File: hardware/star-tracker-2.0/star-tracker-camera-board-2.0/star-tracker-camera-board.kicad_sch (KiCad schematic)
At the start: 41 parts, among them J1 3-1734742-6, U1 AR0134CSSM00SPCA0, U2 TPS70618DRVR, U3 TPS71928-28DRVT, U4 TPS71928-28DRVT, X1 MC2520Z27.0000C19XSH

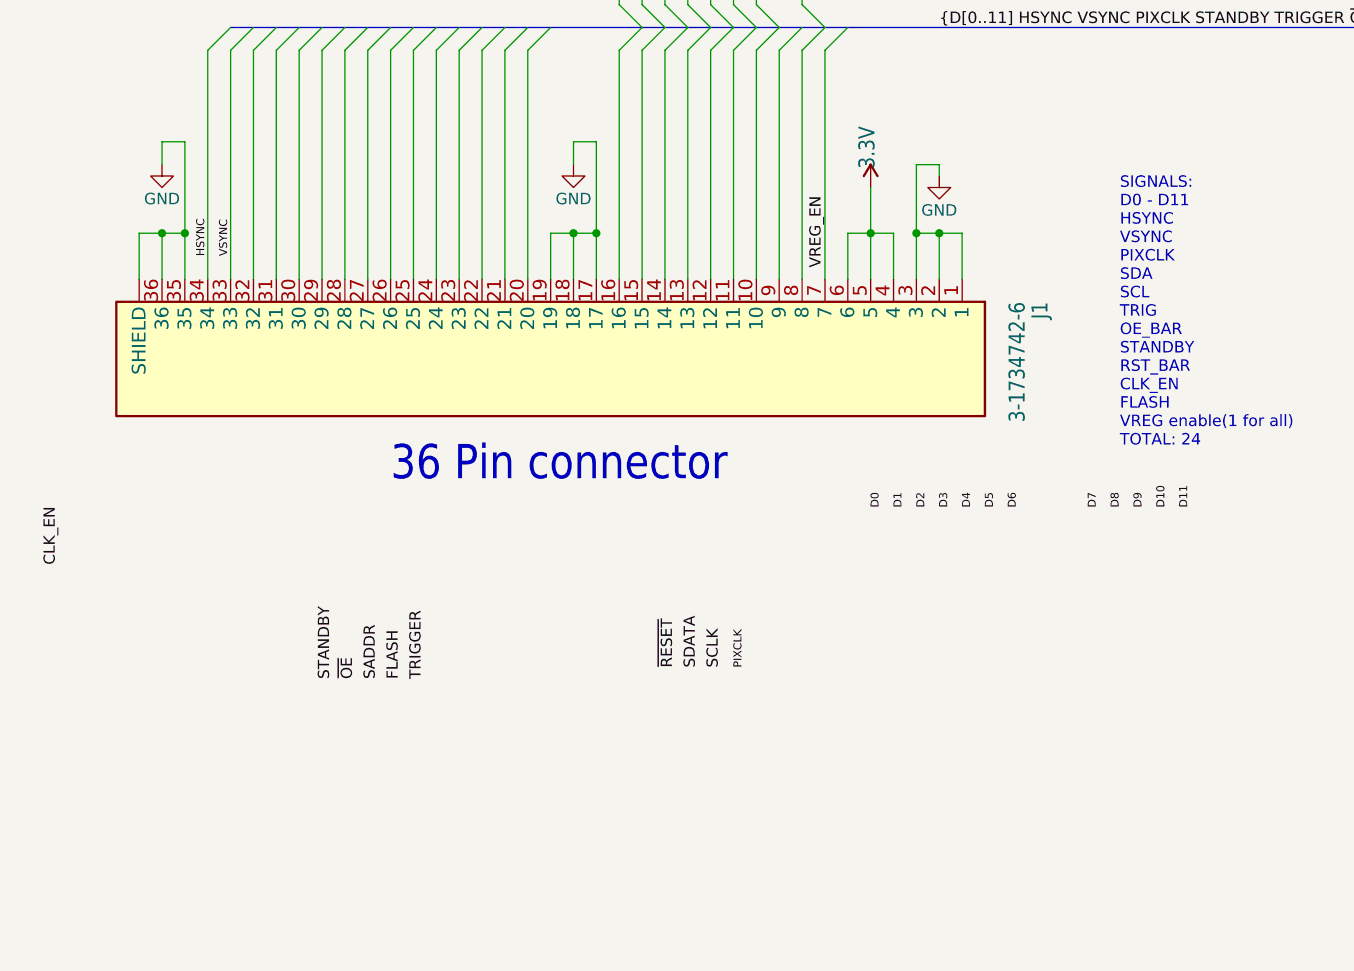
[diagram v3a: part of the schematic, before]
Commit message: Update on camera board
Finished layout and routing. Only needs DRC error fixing and silk screen placement
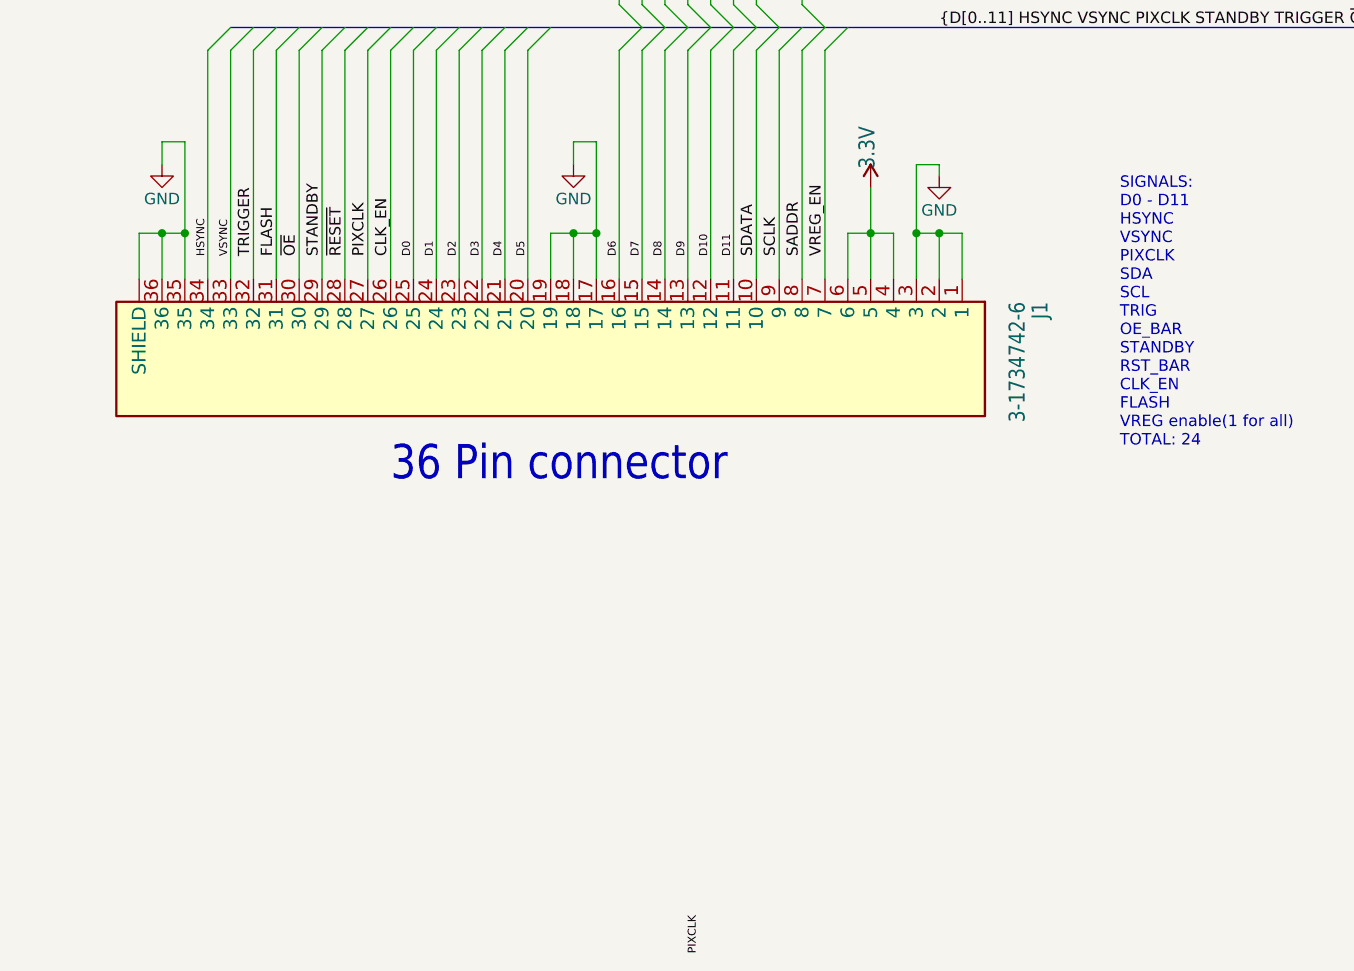
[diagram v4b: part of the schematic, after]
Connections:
- net CLK_EN: now also J1.26
- net D0: now also J1.25
- net D1: now also J1.24
- net D10: now also J1.12
- net D11: now also J1.11
- net D2: now also J1.23
- net D3: now also J1.22
- net D4: now also J1.21
- net D5: now also J1.20
- net D6: now also J1.16
- net D7: now also J1.15
- net D8: now also J1.14
- net D9: now also J1.13
- net FLASH: now also J1.31
- net PIXCLK: now also J1.27
- net SADDR: now also J1.8
- net SCLK: now also J1.9
- net SDATA: now also J1.10
- net STANDBY: now also J1.29
- net TRIGGER: now also J1.32
- net ~{OE}: now also J1.30
- net ~{RESET}: now also J1.28
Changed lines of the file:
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@@
 	(wire
 		(pts
+			(xy 137.16 170.18) (xy 137.16 195.58)
+		)
+		(stroke
+			(width 0.1524)
+			(type solid)
+		)
+	)
+	(wire
+		(pts
 			(xy 116.84 66.04) (xy 116.84 76.2)
 		)
@@
 	(wire
 		(pts
-			(xy 134.62 170.18) (xy 134.62 195.58)
-		)
-		(stroke
-			(width 0)
-			(type default)
-		)
-	)
-	(wire
-		(pts
 			(xy 294.64 53.34) (xy 294.64 55.88)
 		)
@@
 	(wire
 		(pts
-			(xy 137.16 170.18) (xy 137.16 195.58)
-		)
-		(stroke
-			(width 0.1524)
-			(type solid)
-		)
-	)
-	(wire
-		(pts
 			(xy 368.3 134.62) (xy 368.3 132.08)
 		)
@@
 	(wire
 		(pts
+			(xy 134.62 170.18) (xy 134.62 195.58)
+		)
+		(stroke
+			(width 0)
+			(type default)
+		)
+	)
+	(wire
+		(pts
 			(xy 144.78 134.62) (xy 144.78 132.08)
 		)
@@
 		)
 	)
-	(label "D3"
-		(at 151.13 220.98 90)
-		(effects
-			(font
-				(size 0.889 0.889)
-			)
-			(justify left bottom)
-		)
-	)
-	(label "D0"
-		(at 143.51 220.98 90)
-		(effects
-			(font
-				(size 0.889 0.889)
-			)
-			(justify left bottom)
-		)
-	)
 	(label "D0"
 		(at 231.14 73.66 0)
@@
 		)
 	)
-	(label "PIXCLK"
-		(at 128.27 238.76 90)
-		(effects
-			(font
-				(size 0.889 0.889)
-			)
-			(justify left bottom)
-		)
-	)
 	(label "SCLK"
 		(at 166.37 99.06 180)
@@
 		)
 	)
-	(label "D1"
-		(at 146.05 220.98 90)
-		(effects
-			(font
-				(size 0.889 0.889)
-			)
-			(justify left bottom)
-		)
-	)
 	(label "D11"
-		(at 177.8 220.98 90)
+		(at 127 193.04 90)
 		(effects
 			(font
@@
 	)
 	(label "D8"
-		(at 170.18 220.98 90)
+		(at 119.38 193.04 90)
 		(effects
 			(font
@@
 	)
 	(label "VREG_EN"
-		(at 137.16 194.31 90)
+		(at 137.16 193.04 90)
 		(effects
 			(font
@@
 	)
 	(label "TRIGGER"
-		(at 92.71 240.03 90)
+		(at 73.66 193.04 90)
 		(effects
 			(font
@@
 	)
 	(label "D6"
-		(at 158.75 220.98 90)
+		(at 114.3 193.04 90)
+		(effects
+			(font
+				(size 0.889 0.889)
+			)
+			(justify left bottom)
+		)
+	)
+	(label "D1"
+		(at 93.98 193.04 90)
 		(effects
 			(font
@@
 	)
 	(label "SADDR"
-		(at 87.63 240.03 90)
+		(at 134.62 193.04 90)
 		(effects
 			(font
@@
 	)
 	(label "D9"
-		(at 172.72 220.98 90)
+		(at 121.92 193.04 90)
 		(effects
 			(font
@@
 		)
 	)
+	(label "PIXCLK"
+		(at 86.36 193.04 90)
+		(effects
+			(font
+				(size 1.2446 1.2446)
+			)
+			(justify left bottom)
+		)
+	)
 	(label "D7"
-		(at 167.64 220.98 90)
+		(at 116.84 193.04 90)
 		(effects
 			(font
@@
 		)
 	)
-	(label "CLK_EN"
-		(at 52.07 227.33 90)
-		(effects
-			(font
-				(size 1.2446 1.2446)
-			)
-			(justify left bottom)
-		)
-	)
 	(label "SDATA"
 		(at 166.37 101.6 180)
@@
 		)
 	)
-	(label "D2"
-		(at 148.59 220.98 90)
+	(label "STANDBY"
+		(at 81.28 193.04 90)
 		(effects
 			(font
-				(size 0.889 0.889)
+				(size 1.2446 1.2446)
 			)
 			(justify left bottom)
 		)
 	)
-	(label "STANDBY"
-		(at 82.55 240.03 90)
+	(label "SDATA"
+		(at 129.54 193.04 90)
 		(effects
 			(font
@@
 		)
 	)
-	(label "SDATA"
-		(at 123.19 238.76 90)
+	(label "D0"
+		(at 91.44 193.04 90)
 		(effects
 			(font
-				(size 1.2446 1.2446)
+				(size 0.889 0.889)
 			)
 			(justify left bottom)
@@
 	)
 	(label "~{RESET}"
-		(at 120.65 238.76 90)
+		(at 83.82 193.04 90)
+		(effects
+			(font
+				(size 1.2446 1.2446)
+			)
+			(justify left bottom)
+		)
+	)
+	(label "CLK_EN"
+		(at 88.9 193.04 90)
 		(effects
 			(font
@@
 	)
 	(label "D10"
-		(at 175.26 220.98 90)
+		(at 124.46 193.04 90)
+		(effects
+			(font
+				(size 0.889 0.889)
+			)
+			(justify left bottom)
+		)
+	)
+	(label "D4"
+		(at 101.6 193.04 90)
+		(effects
+			(font
+				(size 0.889 0.889)
+			)
+			(justify left bottom)
+		)
+	)
+	(label "D3"
+		(at 99.06 193.04 90)
 		(effects
 			(font
@@
 	)
 	(label "~{OE}"
-		(at 85.09 240.03 90)
+		(at 78.74 193.04 90)
 		(effects
 			(font
@@
 	)
 	(label "FLASH"
-		(at 90.17 240.03 90)
+		(at 76.2 193.04 90)
 		(effects
 			(font
@@
 		)
 	)
+	(label "PIXCLK"
+		(at 123.19 270.51 90)
+		(effects
+			(font
+				(size 0.889 0.889)
+			)
+			(justify left bottom)
+		)
+	)
 	(label "D5"
-		(at 156.21 220.98 90)
+		(at 104.14 193.04 90)
 		(effects
 			(font
@@
 	)
 	(label "SCLK"
-		(at 125.73 238.76 90)
+		(at 132.08 193.04 90)
 		(effects
 			(font
@@
 		)
 	)
+	(label "D2"
+		(at 96.52 193.04 90)
+		(effects
+			(font
+				(size 0.889 0.889)
+			)
+			(justify left bottom)
+		)
+	)
 	(label "D7"
 		(at 231.14 91.44 0)
@@
 		(effects
 			(font
-				(size 0.889 0.889)
-			)
-			(justify left bottom)
-		)
-	)
-	(label "D4"
-		(at 153.67 220.98 90)
-		(effects
-			(font

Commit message: Routine Push
Updated schematic and layout. about 60% done with routing.
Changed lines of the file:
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@@
 		)
 	)
-	(label "{D[0..11] HSYNC VSYNC PIXCLK STANDBY TRIGGER ~{OE} ~{RESET} SCLK SDATA SADDR FLASH VREG_EN}"
-		(at 149.86 167.64 0)
+	(label "{D[0..11] HSYNC VSYNC PIXCLK STANDBY TRIGGER ~{OE} ~{RESET} SCLK SDATA SADDR FLASH VREG_EN CLK_EN}"
+		(at 142.24 167.64 0)
 		(effects
 			(font
@@
 			)
 			(justify left bottom)
-		)
-	)
-	(label "PIXCLK"
-		(at 123.19 270.51 90)
-		(effects
-			(font
-				(size 0.889 0.889)
-			)
-			(justify left bottom)

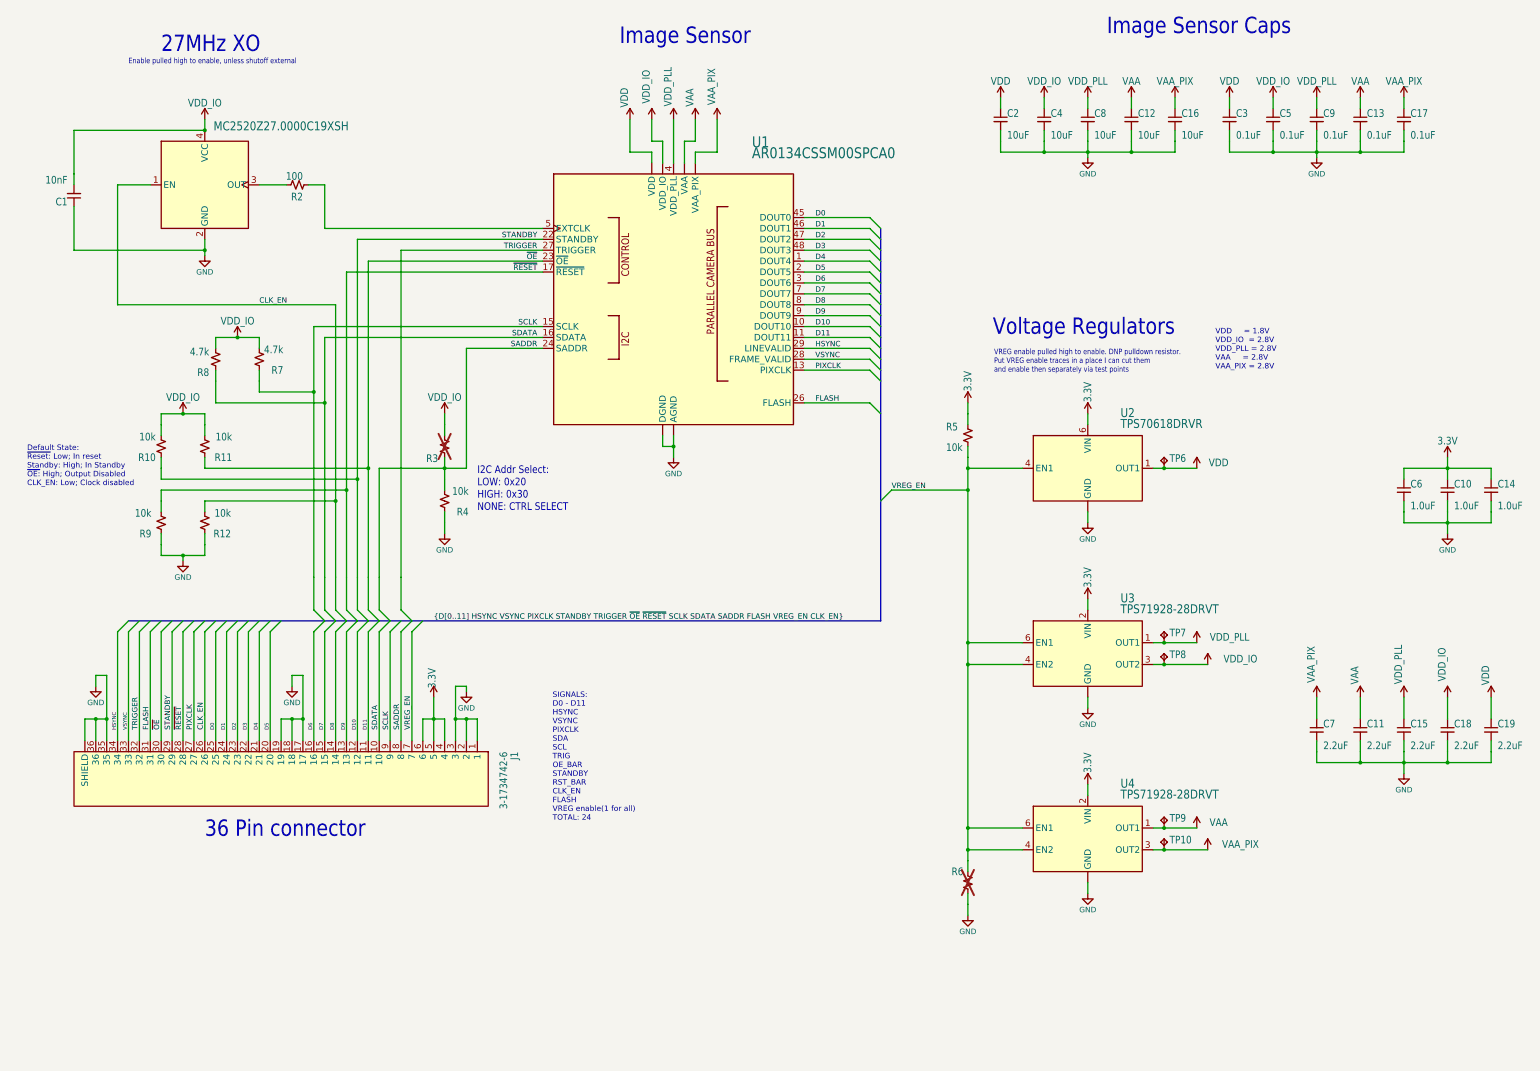
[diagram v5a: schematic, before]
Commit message: Final Cleanup
Added 3d models to camera and star tracker module. Tightened routing and changed power planes as per DR from Friday.
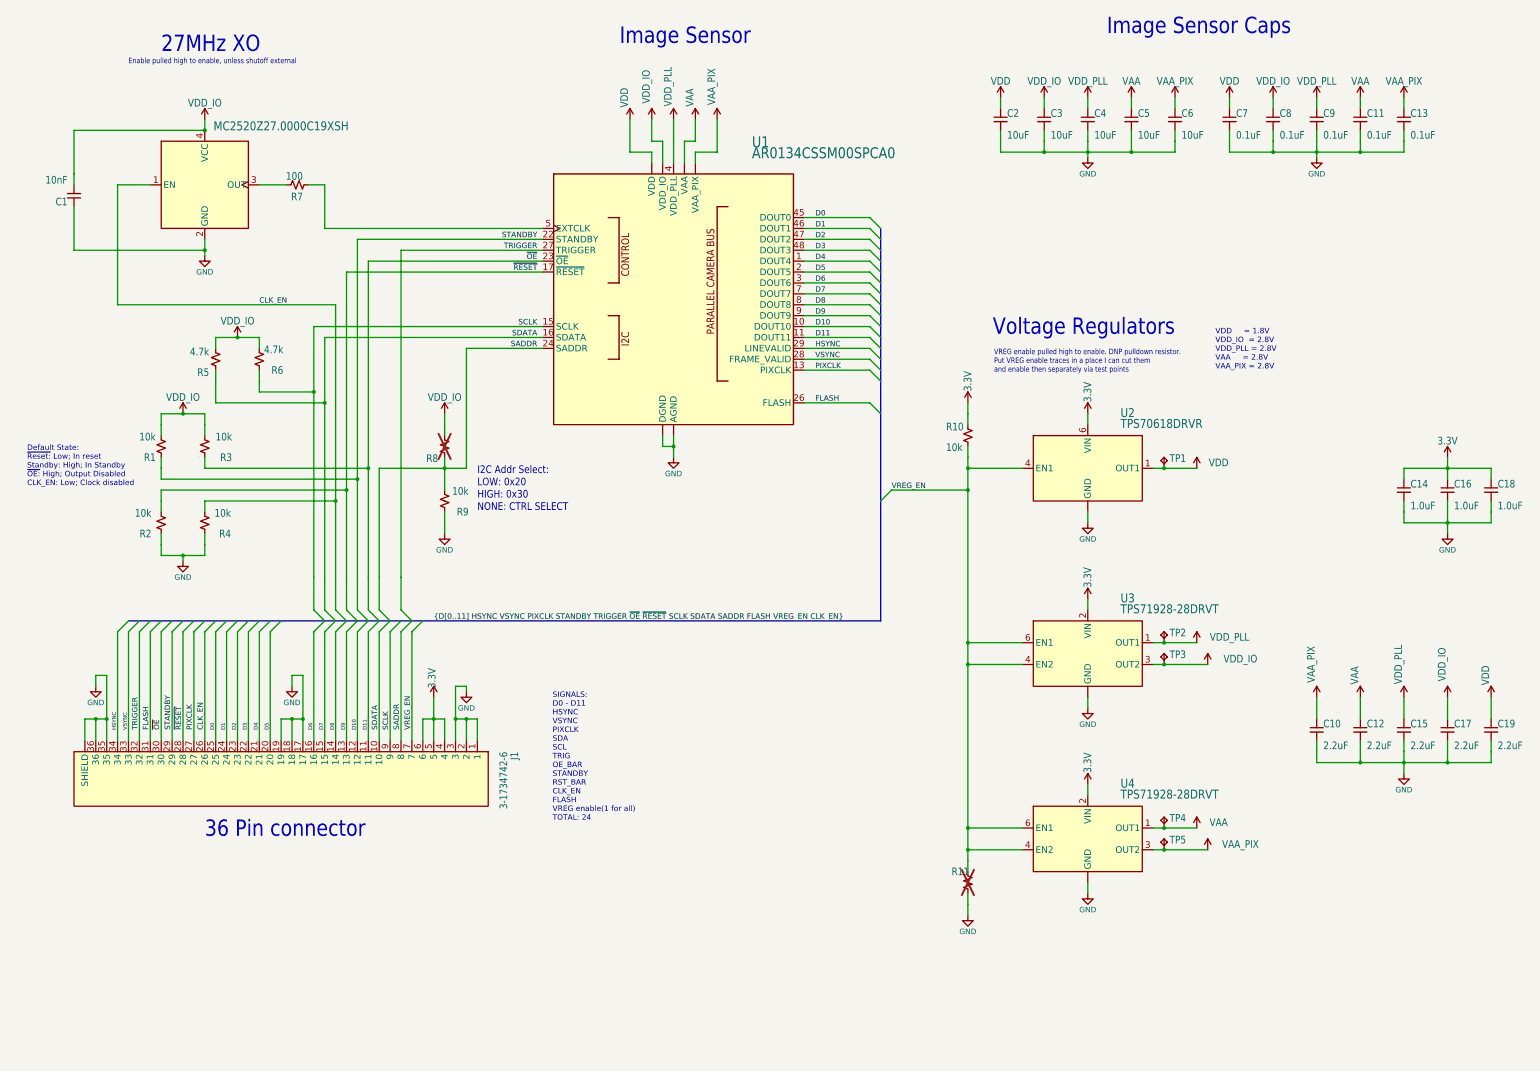
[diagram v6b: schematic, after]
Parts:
- renumbered C7 to C10, C13 to C11, C11 to C12, C17 to C13, C6 to C14, C10 to C16, C18 to C17, C14 to C18, C4 to C3, C8 to C4, C12 to C5, C16 to C6, C3 to C7, C5 to C8, R10 to R1, R5 to R10, R6 to R11, R9 to R2, R11 to R3, R12 to R4, R8 to R5, R7 to R6, R2 to R7, R3 to R8, R4 to R9, TP6 to TP1, TP7 to TP2, TP8 to TP3, TP9 to TP4, TP10 to TP5
